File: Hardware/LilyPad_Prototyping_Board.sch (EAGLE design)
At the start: 138 parts, among them J1 SEWTAP_LONG, J10 SEWTAP_LONG, J11 SEWTAP_LONG, J12 SEWTAP_LONG, J13 SEWTAP_LONG, J14 SEWTAP_LONG, J15 AMP FCI 10103594-0001LF, J2 SEWTAP_LONG, J3 SEWTAP_LONG, J4 SEWTAP_LONG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

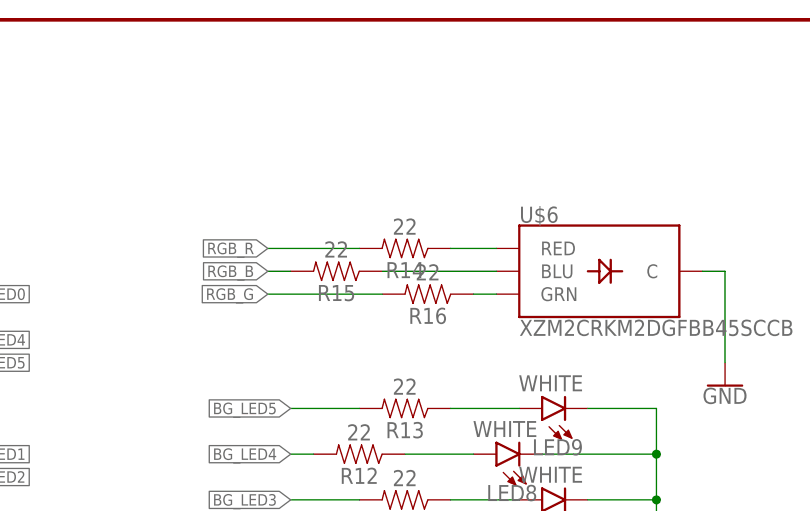
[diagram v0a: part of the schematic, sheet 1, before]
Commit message: Tweaked a couple resistor values
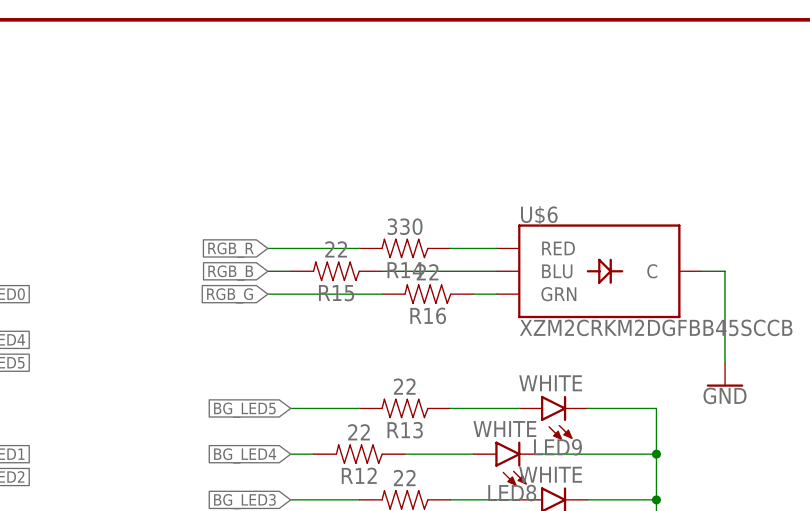
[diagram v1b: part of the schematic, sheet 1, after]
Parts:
- R14: value 22 -> 330; device SparkFun-Resistors:22OHM-0402-1/10W-1% -> SparkFun-Resistors:330OHM-0603-1/10W-1%
- R25, R26, R29, R30: device SparkFun-Resistors:100OHM-0603-1/4W-5% -> SparkFun-Resistors:100OHM-0603-1/10W-1%
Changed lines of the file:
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@@
 <part name="TP4" library="SparkFun-Connectors" deviceset="TEST-POINT" device="3"/>
 <part name="P+6" library="SparkFun-PowerSymbols" deviceset="3.3V" device=""/>
-<part name="R14" library="SparkFun-Resistors" deviceset="22OHM" device="-0402-1/10W-1%" value="22"/>
+<part name="R14" library="SparkFun-Resistors" deviceset="330OHM" device="-0603-1/10W-1%" value="330"/>
 <part name="R15" library="SparkFun-Resistors" deviceset="22OHM" device="-0402-1/10W-1%" value="22"/>
 <part name="R16" library="SparkFun-Resistors" deviceset="22OHM" device="-0402-1/10W-1%" value="22"/>
@@
 <part name="D5" library="SparkFun-LED" deviceset="LED-RED" device="1206" value="RED"/>
 <part name="D6" library="SparkFun-LED" deviceset="LED-RED" device="1206" value="RED"/>
-<part name="R25" library="SparkFun-Resistors" deviceset="100OHM" device="-0603-1/4W-5%" value="100"/>
-<part name="R26" library="SparkFun-Resistors" deviceset="100OHM" device="-0603-1/4W-5%" value="100"/>
+<part name="R25" library="SparkFun-Resistors" deviceset="100OHM" device="-0603-1/10W-1%" value="100"/>
+<part name="R26" library="SparkFun-Resistors" deviceset="100OHM" device="-0603-1/10W-1%" value="100"/>
 <part name="R27" library="SparkFun-Resistors" deviceset="150OHM" device="-0603-1/10W-1%" value="150"/>
 <part name="R28" library="SparkFun-Resistors" deviceset="150OHM" device="-0603-1/10W-1%" value="150"/>
@@
 <part name="D8" library="SparkFun-LED" deviceset="LED-BLUE" device="1206" value="BLUE"/>
 <part name="D9" library="SparkFun-LED" deviceset="LED-BLUE" device="1206" value="BLUE"/>
-<part name="R29" library="SparkFun-Resistors" deviceset="100OHM" device="-0603-1/4W-5%" value="100"/>
-<part name="R30" library="SparkFun-Resistors" deviceset="100OHM" device="-0603-1/4W-5%" value="100"/>
+<part name="R29" library="SparkFun-Resistors" deviceset="100OHM" device="-0603-1/10W-1%" value="100"/>
+<part name="R30" library="SparkFun-Resistors" deviceset="100OHM" device="-0603-1/10W-1%" value="100"/>
 <part name="R31" library="SparkFun-Resistors" deviceset="150OHM" device="-0603-1/10W-1%" value="150"/>
 <part name="R32" library="SparkFun-Resistors" deviceset="150OHM" device="-0603-1/10W-1%" value="150"/>

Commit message: Fixed some stop/lilypad tab errors
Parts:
- J1, J10, J11, J12, J13, J14, J2, J3, J4, J5, J6, J7, J8, J9: value SEWTAP_LONG -> SEWTAP_LONG-2SIDE; device LilyPad-Wearables:SEWTAP_LONG -> LilyPad-Wearables:SEWTAP_LONG-2SIDE
- U$38, U$39: value SEWTAP_SMALL -> SEWTAP_SMALL-2SIDE; device LilyPad-Wearables:SEWTAP_SMALL -> LilyPad-Wearables:SEWTAP_SMALL-2SIDE
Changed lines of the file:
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@@
 <part name="GND12" library="SparkFun-PowerSymbols" deviceset="GND" device=""/>
 <part name="U$5" library="newLilypadParts" deviceset="ATMEGA32U4_NOARD" device="QFN" value="32U4"/>
-<part name="J1" library="LilyPad-Wearables" deviceset="SEWTAP" device="_LONG"/>
-<part name="J2" library="LilyPad-Wearables" deviceset="SEWTAP" device="_LONG"/>
-<part name="J3" library="LilyPad-Wearables" deviceset="SEWTAP" device="_LONG"/>
-<part name="J4" library="LilyPad-Wearables" deviceset="SEWTAP" device="_LONG"/>
-<part name="J5" library="LilyPad-Wearables" deviceset="SEWTAP" device="_LONG"/>
-<part name="J6" library="LilyPad-Wearables" deviceset="SEWTAP" device="_LONG"/>
-<part name="J7" library="LilyPad-Wearables" deviceset="SEWTAP" device="_LONG"/>
-<part name="J8" library="LilyPad-Wearables" deviceset="SEWTAP" device="_LONG"/>
-<part name="J9" library="LilyPad-Wearables" deviceset="SEWTAP" device="_LONG"/>
-<part name="J10" library="LilyPad-Wearables" deviceset="SEWTAP" device="_LONG"/>
-<part name="J11" library="LilyPad-Wearables" deviceset="SEWTAP" device="_LONG"/>
-<part name="J12" library="LilyPad-Wearables" deviceset="SEWTAP" device="_LONG"/>
-<part name="J13" library="LilyPad-Wearables" deviceset="SEWTAP" device="_LONG"/>
-<part name="J14" library="LilyPad-Wearables" deviceset="SEWTAP" device="_LONG"/>
+<part name="J1" library="LilyPad-Wearables" deviceset="SEWTAP" device="_LONG-2SIDE" value="SEWTAP_LONG-2SIDE"/>
+<part name="J2" library="LilyPad-Wearables" deviceset="SEWTAP" device="_LONG-2SIDE" value="SEWTAP_LONG-2SIDE"/>
+<part name="J3" library="LilyPad-Wearables" deviceset="SEWTAP" device="_LONG-2SIDE" value="SEWTAP_LONG-2SIDE"/>
+<part name="J4" library="LilyPad-Wearables" deviceset="SEWTAP" device="_LONG-2SIDE" value="SEWTAP_LONG-2SIDE"/>
+<part name="J5" library="LilyPad-Wearables" deviceset="SEWTAP" device="_LONG-2SIDE" value="SEWTAP_LONG-2SIDE"/>
+<part name="J6" library="LilyPad-Wearables" deviceset="SEWTAP" device="_LONG-2SIDE" value="SEWTAP_LONG-2SIDE"/>
+<part name="J7" library="LilyPad-Wearables" deviceset="SEWTAP" device="_LONG-2SIDE" value="SEWTAP_LONG-2SIDE"/>
+<part name="J8" library="LilyPad-Wearables" deviceset="SEWTAP" device="_LONG-2SIDE" value="SEWTAP_LONG-2SIDE"/>
+<part name="J9" library="LilyPad-Wearables" deviceset="SEWTAP" device="_LONG-2SIDE" value="SEWTAP_LONG-2SIDE"/>
+<part name="J10" library="LilyPad-Wearables" deviceset="SEWTAP" device="_LONG-2SIDE" value="SEWTAP_LONG-2SIDE"/>
+<part name="J11" library="LilyPad-Wearables" deviceset="SEWTAP" device="_LONG-2SIDE" value="SEWTAP_LONG-2SIDE"/>
+<part name="J12" library="LilyPad-Wearables" deviceset="SEWTAP" device="_LONG-2SIDE" value="SEWTAP_LONG-2SIDE"/>
+<part name="J13" library="LilyPad-Wearables" deviceset="SEWTAP" device="_LONG-2SIDE" value="SEWTAP_LONG-2SIDE"/>
+<part name="J14" library="LilyPad-Wearables" deviceset="SEWTAP" device="_LONG-2SIDE" value="SEWTAP_LONG-2SIDE"/>
 <part name="U$6" library="newLilypadParts" deviceset="SUNLED" device="SMD1" value="XZM2CRKM2DGFBB45SCCB"/>
 <part name="LED5" library="SparkFun-LED" deviceset="LED-WHITE" device="0603" value="WHITE"/>
@@
 <part name="U$36" library="LilyPad-Wearables" deviceset="SEWTAP-NOHOLE" device="_SM_NH" value="SEWTAP-NOHOLE_SM_NH"/>
 <part name="U$37" library="LilyPad-Wearables" deviceset="SEWTAP-NOHOLE" device="_SM_NH" value="SEWTAP-NOHOLE_SM_NH"/>
-<part name="U$38" library="LilyPad-Wearables" deviceset="SEWTAP" device="_SMALL" value="SEWTAP_SMALL"/>
-<part name="U$39" library="LilyPad-Wearables" deviceset="SEWTAP" device="_SMALL" value="SEWTAP_SMALL"/>
+<part name="U$38" library="LilyPad-Wearables" deviceset="SEWTAP" device="_SMALL-2SIDE" value="SEWTAP_SMALL-2SIDE"/>
+<part name="U$39" library="LilyPad-Wearables" deviceset="SEWTAP" device="_SMALL-2SIDE" value="SEWTAP_SMALL-2SIDE"/>
 <part name="U$40" library="LilyPad-Wearables" deviceset="SEWTAP-NOHOLE" device="_SM_NH" value="SEWTAP-NOHOLE_SM_NH"/>
 <part name="B1" library="SparkFun-Electromechanical" deviceset="BUZZER" device="-SMD" value="Buzzer"/>

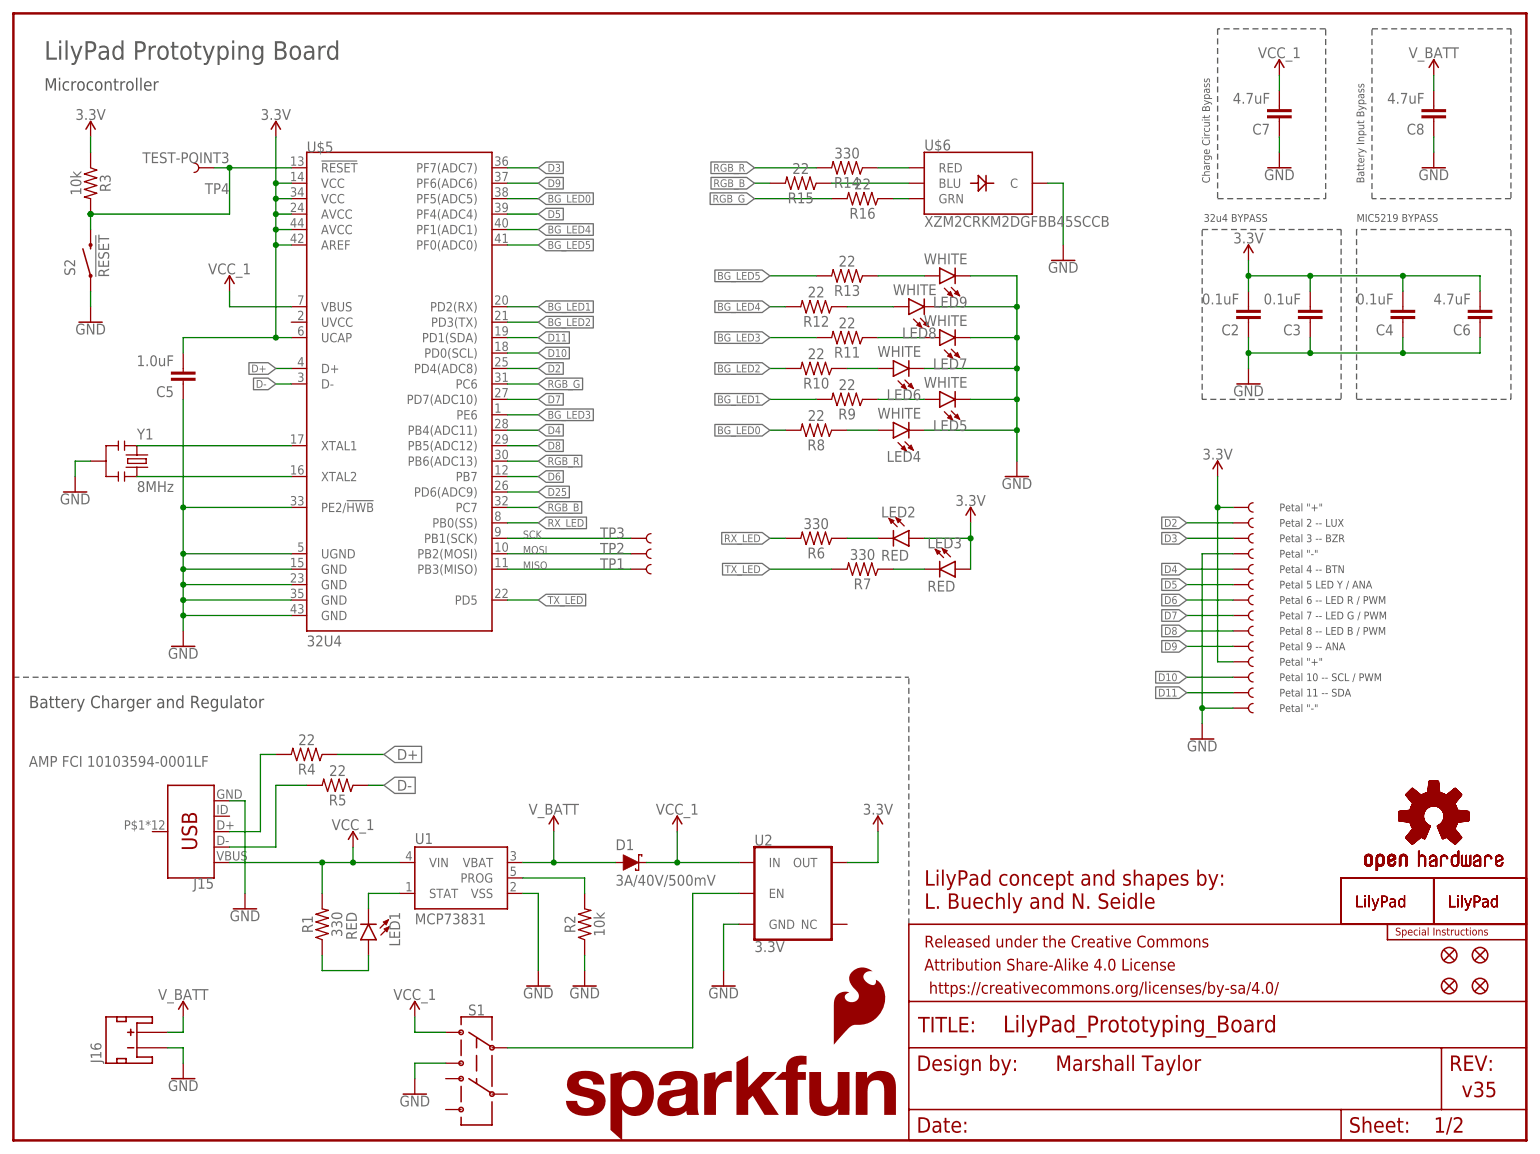
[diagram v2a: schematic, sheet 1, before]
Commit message: Addressed DFM errors
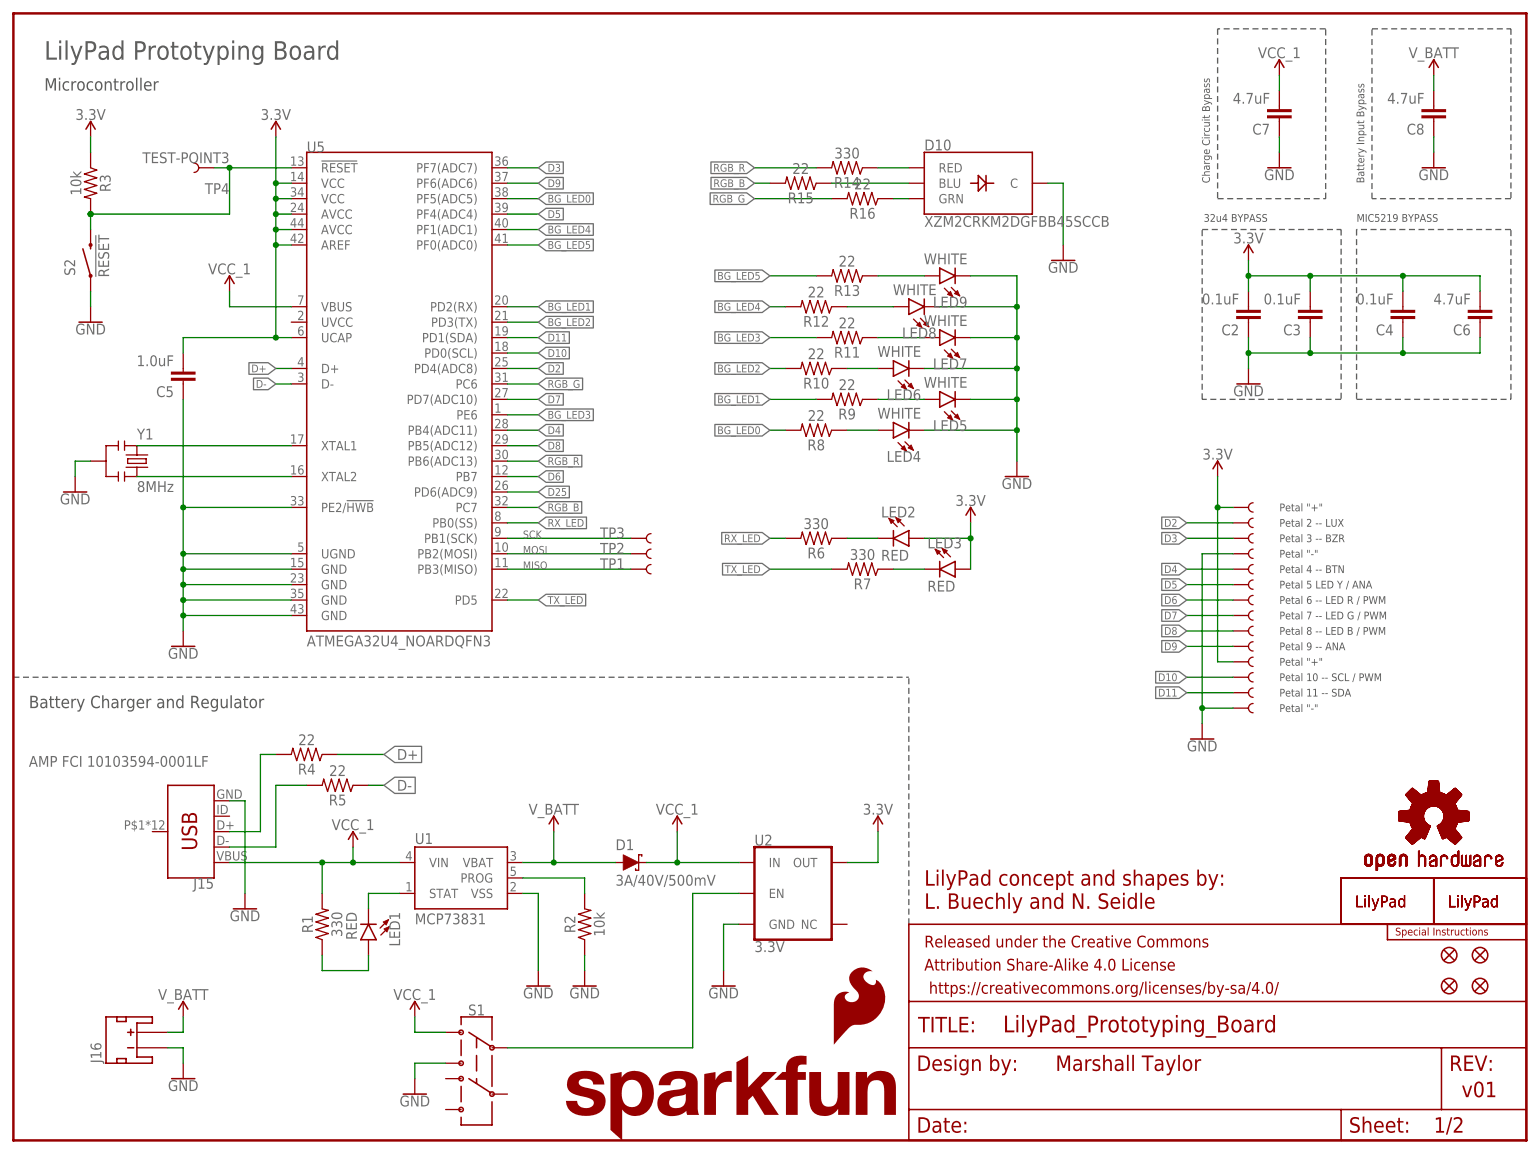
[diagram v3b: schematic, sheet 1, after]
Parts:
- removed U$5: 32U4, newLilypadParts:ATMEGA32U4_NOARDQFN
- removed U$6: XZM2CRKM2DGFBB45SCCB, newLilypadParts:SUNLEDSMD1
- added D10: XZM2CRKM2DGFBB45SCCB, newLilypadParts:SUNLEDSMD1
- added U5: ATMEGA32U4_NOARDQFN3, newLilypadParts:ATMEGA32U4_NOARDQFN3
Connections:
- net 3.3V: now also U5.AREF, U5.AVCC@24, U5.AVCC@44, U5.UCAP, U5.VCC@14, U5.VCC@34; no longer U$5.AREF, U$5.AVCC@24, U$5.AVCC@44, U$5.UCAP, U$5.VCC@14, U$5.VCC@34
- net BG_LED0: now also U5.PF5(ADC5); no longer U$5.PF5(ADC5)
- net BG_LED1: now also U5.PD2(RX); no longer U$5.PD2(RX)
- net BG_LED2: now also U5.PD3(TX); no longer U$5.PD3(TX)
- net BG_LED3: now also U5.PE6; no longer U$5.PE6
- net BG_LED4: now also U5.PF1(ADC1); no longer U$5.PF1(ADC1)
- net BG_LED5: now also U5.PF0(ADC0); no longer U$5.PF0(ADC0)
- net D+: now also U5.D+; no longer U$5.D+
- net D-: now also U5.D-; no longer U$5.D-
- net D10: now also U5.PD0(SCL); no longer U$5.PD0(SCL)
- net D11: now also U5.PD1(SDA); no longer U$5.PD1(SDA)
- net D2: now also U5.PD4(ADC8); no longer U$5.PD4(ADC8)
- net D25: now also U5.PD6(ADC9); no longer U$5.PD6(ADC9)
- net D3: now also U5.PF7(ADC7); no longer U$5.PF7(ADC7)
- net D4: now also U5.PB4(ADC11); no longer U$5.PB4(ADC11)
- net D5: now also U5.PF4(ADC4); no longer U$5.PF4(ADC4)
- net D6: now also U5.PB7; no longer U$5.PB7
- net D7: now also U5.PD7(ADC10); no longer U$5.PD7(ADC10)
- net D8: now also U5.PB5(ADC12); no longer U$5.PB5(ADC12)
- net D9: now also U5.PF6(ADC6); no longer U$5.PF6(ADC6)
- net GND: now also D10.C, U5.GND@15, U5.GND@23, U5.GND@35, U5.GND@43, U5.PE2/!HWB, U5.UGND; no longer U$5.GND@15, U$5.GND@23, U$5.GND@35, U$5.GND@43, U$5.PE2/!HWB, U$5.UGND, U$6.C
- net MISO: now also U5.PB3(MISO); no longer U$5.PB3(MISO)
- net MOSI: now also U5.PB2(MOSI); no longer U$5.PB2(MOSI)
- net N$14: now also D10.BLU; no longer U$6.BLU
- net N$15: now also D10.RED; no longer U$6.RED
- net N$5: now also U5.XTAL1; no longer U$5.XTAL1
- net N$7: now also U5.XTAL2; no longer U$5.XTAL2
- net N$8: now also D10.GRN; no longer U$6.GRN
- net RESET: now also U5.!RESET; no longer U$5.!RESET
- net RGB_B: now also U5.PC7; no longer U$5.PC7
- net RGB_G: now also U5.PC6; no longer U$5.PC6
- net RGB_R: now also U5.PB6(ADC13); no longer U$5.PB6(ADC13)
- net RX_LED: now also U5.PB0(SS); no longer U$5.PB0(SS)
- net SCK: now also U5.PB1(SCK); no longer U$5.PB1(SCK)
- net TX_LED: now also U5.PD5; no longer U$5.PD5
- net VCC_1: now also U5.VBUS; no longer U$5.VBUS
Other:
- note added: "v01"
- note removed: "v35"
